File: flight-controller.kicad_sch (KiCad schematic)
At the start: 66 parts, among them J1 USB_C_Receptacle_USB2.0, Q1 AO3400A, SW1 SW_Push, U1 AT32F435RGT7, U2 BMI270, U3 BMP280, U4 W25N01GVZEIG, U5 AT7456E, U6 TPS54302, U7 TPS54302, U8 TLV75733PDBV, U9 USBLC6-2P6, Y1 27MHz

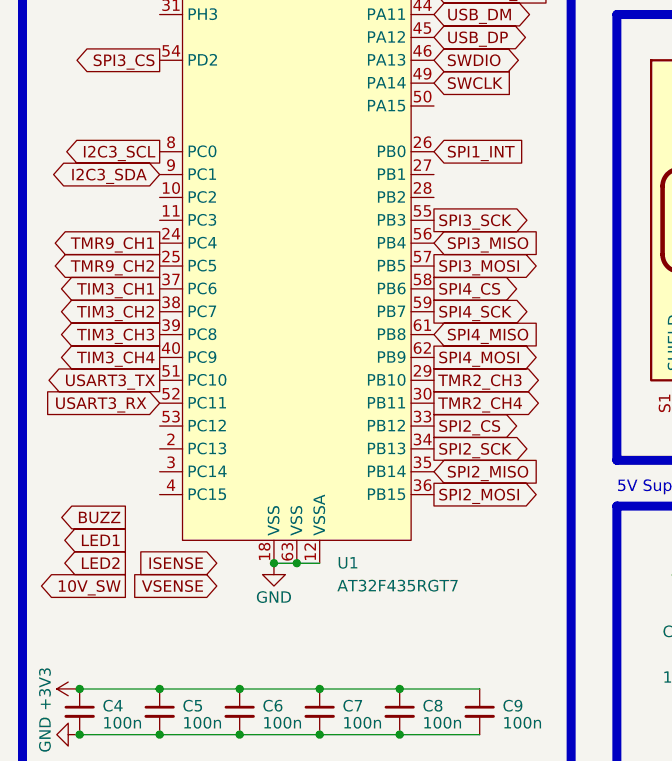
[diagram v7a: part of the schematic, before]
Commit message: Assign remaining peripherals to AT32 pins
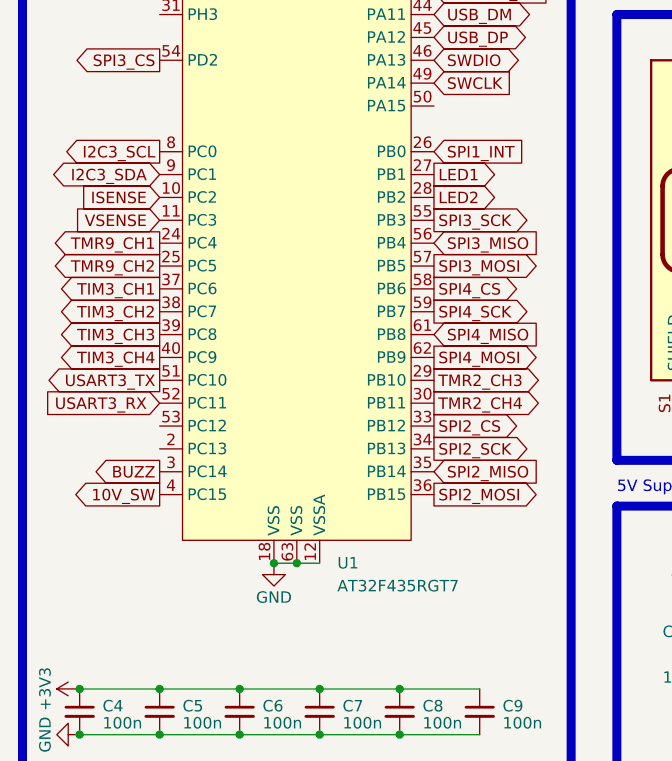
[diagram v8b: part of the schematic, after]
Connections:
- net 10V_SW: now also U1.4 (PC15)
- net BUZZ: now also U1.3 (PC14)
- net ISENSE: now also U1.10 (PC2)
- net LED1: now also U1.27 (PB1)
- net LED2: now also U1.28 (PB2)
- net VSENSE: now also U1.11 (PC3)
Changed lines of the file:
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@@
     )
   )
-  (global_label "LED2" (shape output) (at 26.67 124.46 180) (fields_autoplaced)
-    (effects (font (size 1.27 1.27)) (justify right))
-    (property "Intersheetrefs" "${INTERSHEET_REFS}" (at 19.1076 124.46 0)
-      (effects (font (size 1.27 1.27)) (justify right) hide)
+  (global_label "LED2" (shape output) (at 60.96 83.82 0) (fields_autoplaced)
+    (effects (font (size 1.27 1.27)) (justify left))
+    (property "Intersheetrefs" "${INTERSHEET_REFS}" (at 68.5224 83.82 0)
+      (effects (font (size 1.27 1.27)) (justify left) hide)
     )
   )
@@
     )
   )
-  (global_label "10V_SW" (shape output) (at 26.67 127 180) (fields_autoplaced)
-    (effects (font (size 1.27 1.27)) (justify right))
-    (property "Intersheetrefs" "${INTERSHEET_REFS}" (at 16.6281 127 0)
+  (global_label "10V_SW" (shape output) (at 30.48 116.84 180) (fields_autoplaced)
+    (effects (font (size 1.27 1.27)) (justify right))
+    (property "Intersheetrefs" "${INTERSHEET_REFS}" (at 20.4381 116.84 0)
       (effects (font (size 1.27 1.27)) (justify right) hide)
     )
@@
     )
   )
-  (global_label "ISENSE" (shape input) (at 36.83 124.46 180) (fields_autoplaced)
-    (effects (font (size 1.27 1.27)) (justify right))
-    (property "Intersheetrefs" "${INTERSHEET_REFS}" (at 27.2719 124.46 0)
+  (global_label "ISENSE" (shape input) (at 30.48 83.82 180) (fields_autoplaced)
+    (effects (font (size 1.27 1.27)) (justify right))
+    (property "Intersheetrefs" "${INTERSHEET_REFS}" (at 20.9219 83.82 0)
       (effects (font (size 1.27 1.27)) (justify right) hide)
     )
@@
     )
   )
-  (global_label "LED1" (shape output) (at 26.67 121.92 180) (fields_autoplaced)
-    (effects (font (size 1.27 1.27)) (justify right))
-    (property "Intersheetrefs" "${INTERSHEET_REFS}" (at 19.1076 121.92 0)
-      (effects (font (size 1.27 1.27)) (justify right) hide)
+  (global_label "LED1" (shape output) (at 60.96 81.28 0) (fields_autoplaced)
+    (effects (font (size 1.27 1.27)) (justify left))
+    (property "Intersheetrefs" "${INTERSHEET_REFS}" (at 68.5224 81.28 0)
+      (effects (font (size 1.27 1.27)) (justify left) hide)
     )
   )
@@
     )
   )
-  (global_label "VSENSE" (shape input) (at 36.83 127 180) (fields_autoplaced)
-    (effects (font (size 1.27 1.27)) (justify right))
-    (property "Intersheetrefs" "${INTERSHEET_REFS}" (at 26.7881 127 0)
-      (effects (font (size 1.27 1.27)) (justify right) hide)
-    )
-  )
-  (global_label "BUZZ" (shape output) (at 26.67 119.38 180) (fields_autoplaced)
-    (effects (font (size 1.27 1.27)) (justify right))
-    (property "Intersheetrefs" "${INTERSHEET_REFS}" (at 18.7447 119.38 0)
-      (effects (font (size 1.27 1.27)) (justify right) hide)
-    )
+  (global_label "VSENSE" (shape input) (at 30.48 86.36 180) (fields_autoplaced)
+    (effects (font (size 1.27 1.27)) (justify right))
+    (property "Intersheetrefs" "${INTERSHEET_REFS}" (at 20.4381 86.36 0)
+      (effects (font (size 1.27 1.27)) (justify right) hide)
+    )
+  )
+  (global_label "BUZZ" (shape output) (at 30.48 114.3 180) (fields_autoplaced)
+    (effects (font (size 1.27 1.27)) (justify right))
+    (property "Intersheetrefs" "${INTERSHEET_REFS}" (at 22.5547 114.3 0)
+      (effects (font (size 1.27 1.27)) (justify right) hide)
+    )
